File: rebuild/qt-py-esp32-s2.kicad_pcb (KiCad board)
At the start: 2 copper layers, 0 parts

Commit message: gate3: PCB placement — 45/45 placed, 17.78x20.701 outline, DRC run
- qt-py footprint library extracted from the imported board (14 footprints)
- pad names preserved: A/A'/B/B', 1C..7C, A1B12/A4B9/A6/B6, MT1/MT2, C/A, 1/3, FP, P$1, TP
- create_board_from_schematic: 45 footprints, 34 nets, 159 pads assigned
- placement copied from the imported board: 45/45 exact x/y/rotation/layer
- outline 17.78 x 20.701 (8 Edge.Cuts segments), 2 fiducials, no frame
- Eagle rules: 6 mil clearance/width, 15.5 mil drill, 25% annulus, 0.254 edge, 2L 1.6mm
- fixed castellation pad rotation (importer stored 270/90): shorts 26 -> 2
- ERC footprint_link_issues 17 -> 0; annotation warning cleared via GND0/VBAT0
- DRC: 236 violations (37 errors, 199 warnings), 111 unconnected (unrouted)
- renders: 3D top/bottom, 2D
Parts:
- added C1: 22uF, Capacitor_SMD:C_0805_2012Metric, F.Cu at (11.9, -12.7)
- added C10: 0.1uF, Capacitor_SMD:C_0402_1005Metric, B.Cu at (8.43, -14.2)
- added C11: 0.1uF, Capacitor_SMD:C_0402_1005Metric, B.Cu at (14.7, -15.1)
- added C12: 0.1uF, Capacitor_SMD:C_0402_1005Metric, B.Cu at (14.7, -10.9)
- added C13: 1uF, Capacitor_SMD:C_0402_1005Metric, B.Cu at (14.7, -12.9)
- added C14: 0.1uF, Capacitor_SMD:C_0402_1005Metric, B.Cu at (13.0, -2.29)
- added C15: 1uF, Capacitor_SMD:C_0402_1005Metric, B.Cu at (8.84, -3.62)
- added C16: 100pF, Capacitor_SMD:C_0402_1005Metric, B.Cu at (7.95, -3.62)
- added C17: 16pF, Capacitor_SMD:C_0402_1005Metric, B.Cu at (8.48, -2.08)
- added C18: 16pF, Capacitor_SMD:C_0402_1005Metric, B.Cu at (12.1, -2.26)
- added C19: 1uF, Capacitor_SMD:C_0402_1005Metric, B.Cu at (6.48, -14.0)
- added C2: 1uF, Capacitor_SMD:C_0402_1005Metric, B.Cu at (4.38, -9.86)
- added C20: 1uF, Capacitor_SMD:C_0402_1005Metric, B.Cu at (3.11, -12.9)
- added C3: 1uF, Capacitor_SMD:C_0402_1005Metric, B.Cu at (14.3, -2.10)
- added C4: 0.1uF, Capacitor_SMD:C_0402_1005Metric, B.Cu at (4.36, -8.92)
- added C5: 1uF, Capacitor_SMD:C_0402_1005Metric, B.Cu at (7.45, -14.2)
- added C6: 22uF, Capacitor_SMD:C_0805_2012Metric, F.Cu at (13.4, -9.80)
- added C7: TBD, Capacitor_SMD:C_0402_1005Metric, B.Cu at (4.17, -6.91)
- added C8: 22uF, Capacitor_SMD:C_0805_2012Metric, F.Cu at (10.5, -6.93)
- added C9: TBD, Capacitor_SMD:C_0402_1005Metric, B.Cu at (4.18, -5.78)
- added CONN1: STEMMA_I2C_QTSKINNY, qt-py:JST_SH4_SKINNY, F.Cu at (11.1, -2.58)
- added D1: NSR0320, qt-py:SOD-323_MINI, B.Cu at (12.5, -16.8)
- added D2: NSR0320, qt-py:SOD-323_MINI, B.Cu at (14.4, -18.9)
- added FID1: FIDUCIAL_1MM, qt-py:FIDUCIAL_1MM, F.Cu at (6.20, -19.5)
- added FID2: FIDUCIAL_1MM, qt-py:FIDUCIAL_1MM, F.Cu at (10.9, -0.76)
- added GND0: TESTPOINT_P, qt-py:TESTPOINT_MINUS_1X3MM, B.Cu at (6.99, -18.9)
- added JP1: HEADER_1X7, qt-py:1X07_CASTEL, F.Cu at (1.27, -10.4)
- added JP3: HEADER_1X7, qt-py:1X07_CASTEL, F.Cu at (16.5, -10.4)
- added L1: 2nH, Inductor_SMD:L_0402_1005Metric, B.Cu at (4.50, -7.92)
- added L2: 0 ohm, Inductor_SMD:L_0402_1005Metric, B.Cu at (5.69, -6.26)
- added LED1: WS2812B_SK6805_1515, qt-py:SK6805_1515, F.Cu at (13.1, -7.00)
- added Q1: BOOT0, qt-py:BTN_KMR2_4.6X2.8, F.Cu at (6.10, -11.0)
- added Q2: reset, qt-py:BTN_KMR2_4.6X2.8, F.Cu at (6.10, -7.11)
- added R1: 10K, Resistor_SMD:R_0402_1005Metric, B.Cu at (14.3, -2.98)
- added R17: 1Meg, Resistor_SMD:R_0402_1005Metric, B.Cu at (4.00, -12.9)
- added R2: 10K, Resistor_SMD:R_0402_1005Metric, B.Cu at (3.51, -17.1)
- added R3: 0, Resistor_SMD:R_0402_1005Metric, B.Cu at (10.6, -4.58)
- added R5: 5.1K, Resistor_SMD:R_0402_1005Metric, F.Cu at (7.30, -13.1)
- added R6: 5.1K, Resistor_SMD:R_0402_1005Metric, F.Cu at (9.27, -12.9)
- added SWC1: TPB1,27, qt-py:B1_27, B.Cu at (15.6, -0.95)
- added SWC2: TPB1,27, qt-py:B1_27, B.Cu at (2.26, -19.7)
- added U$15: ESP32-S2FN4R2, qt-py:QFN56_7X7, B.Cu at (10.3, -9.19)
- added U1: AP2112K-3.3, qt-py:SOT23-5, F.Cu at (10.9, -9.87)
- added VBAT0: TESTPOINT_P, qt-py:TESTPOINT_PLUS_1X3MM, B.Cu at (10.8, -18.9)
- added X1: ANTENNA_FP, qt-py:ANT_2450AT18B100, F.Cu at (4.83, -1.33)
- added X6: USB TYPE C, qt-py:USB_C_CUSB31-CFM2AX-01-X, F.Cu at (8.89, -17.9)
- added Y1: 40MHz, qt-py:CRYSTAL_2X1.6, B.Cu at (10.5, -2.77)
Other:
- board outline added: 17.8 x 20.7 mm

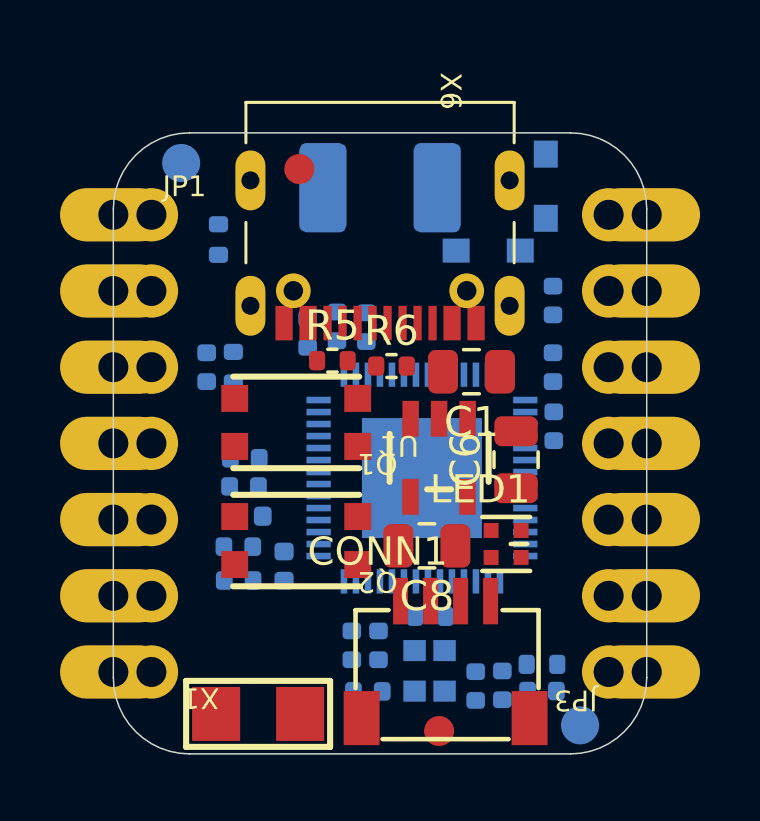
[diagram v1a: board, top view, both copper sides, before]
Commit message: gate4: routing — 0 DRC errors, 20 unconnected documented
preconditions:
- testpoint no-net copper polygon -> equivalent P$1 pad; courtyard closed
- removed ${TP_SIGNAL_NAME} from B1_27 and placed SWC instances
- USB-C NPTH resized 1.158 -> 0.65 mm to match Eagle drill
- documented waivers: castellation edge, USB-C internal holes, courtyard overlap

routing:
- Freerouting 2.5.0, 200 passes, 18 threads; 125 -> 24 unrouted; SES imported
- GND pours on F.Cu/B.Cu, solid pad connection
- 323 segments, 18 vias, 298.86 mm total
- DRC 0 errors, 196 cosmetic warnings, 20 unconnected (13 GND, 4 +3V3, 2 VBUS, 1 IO0)

honest shortfall:
- 20 connections remain unrouted; not intentional
- D+/D- skew 3.51 mm (original 1.10 mm), not length-matched
- lower total length reflects missing links + poured GND, not a better layout
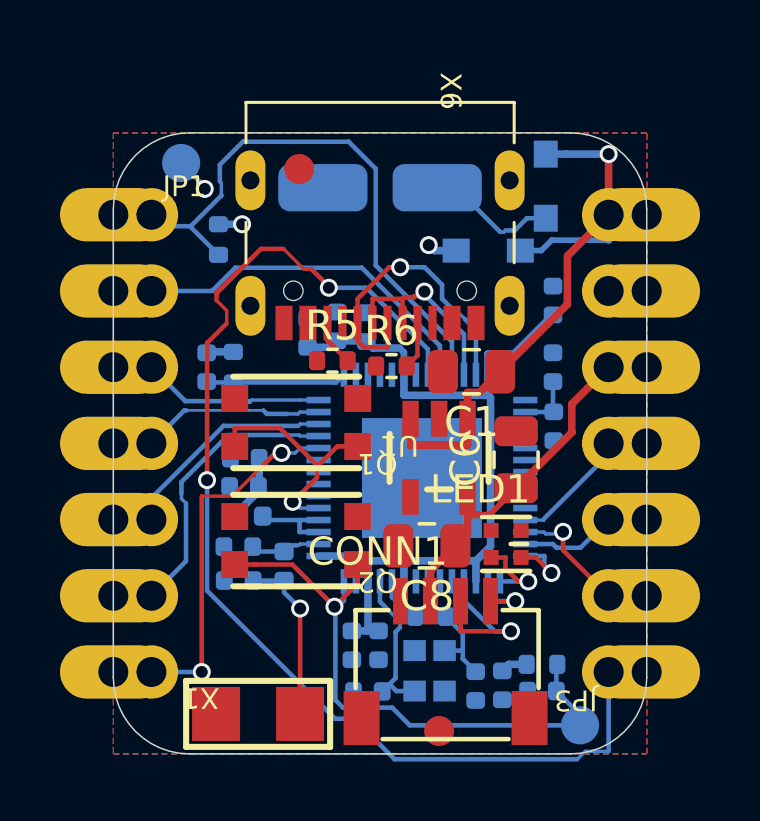
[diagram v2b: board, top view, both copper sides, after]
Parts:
- GND0: value TESTPOINT_P -> TESTPOINT_MINUS_1X3MM
- VBAT0: value TESTPOINT_P -> TESTPOINT_PLUS_1X3MM
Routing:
- net +3V3: track 0.00 -> 44.0 mm, vias 0 -> 1
- net RX: track 0.00 -> 40.0 mm, vias 0 -> 2
- net +5V: track 0.00 -> 22.0 mm, vias 0 -> 1
- net RESET_N: track 0.00 -> 20.7 mm, vias 0 -> 1
- net A0: track 0.00 -> 20.4 mm
- net TX: track 0.00 -> 13.4 mm, vias 0 -> 2
- net A1: track 0.00 -> 13.2 mm
- net SCL: track 0.00 -> 10.8 mm
- net D+: track 0.00 -> 10.3 mm, vias 0 -> 1
- net IO0: track 0.00 -> 9.27 mm, vias 0 -> 2
- net SDA: track 0.00 -> 8.58 mm
- net A3: track 0.00 -> 7.37 mm
- net A2: track 0.00 -> 7.35 mm
- net D-: track 0.00 -> 6.79 mm, vias 0 -> 1
- net RF_ANT: track 0.00 -> 5.70 mm, vias 0 -> 1
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- added copper zone on B.Cu, net GND
- added copper zone on F.Cu, net GND

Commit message: gate4b WIP: GND stitching 20->14, blocked on pour-island links
- 7 stitching vias at F/B fill intersections; main pours merged
- cleared CONN1.MT1/C17.2 and X6 zone links
- 20 -> 14 unconnected, 0 DRC errors, no new waivers
- remaining 7 GND links separated by our signal tracks; need signal reroute
- +3V3 reference geometry tried: 13 unconnected but 36 errors; reverted
- USB-C NPTH 0.65 mm source reference retained
- still NOT COMPLETE; no Gerbers/fabrication
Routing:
- net GND: vias 0 -> 8
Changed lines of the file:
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@@
 		(net "+5V")
+	)
+	(via
+		(at 8 -11.5)
+		(size 0.6)
+		(drill 0.4)
+		(layers "F.Cu" "B.Cu")
+		(net "GND")
+	)
+	(via
+		(at 8 -7.5)
+		(size 0.6)
+		(drill 0.4)
+		(layers "F.Cu" "B.Cu")
+		(net "GND")
+	)
+	(via
+		(at 11 -11)
+		(size 0.6)
+		(drill 0.4)
+		(layers "F.Cu" "B.Cu")
+		(net "GND")
+	)
+	(via
+		(at 4 -13.5)
+		(size 0.6)
+		(drill 0.4)
+		(layers "F.Cu" "B.Cu")
+		(net "GND")
+	)
+	(via
+		(at 12.5 -2)
+		(size 0.6)
+		(drill 0.4)
+		(layers "F.Cu" "B.Cu")
+		(net "GND")
+	)
+	(via
+		(at 8 -2.5)
+		(size 0.6)
+		(drill 0.4)
+		(layers "F.Cu" "B.Cu")
+		(net "GND")
+	)
+	(via
+		(at 8.5 -11.5)
+		(size 0.6)
+		(drill 0.4)
+		(layers "F.Cu" "B.Cu")
+		(net "GND")
+	)
+	(via
+		(at 15 -13.5)
+		(size 0.6)
+		(drill 0.4)
+		(layers "F.Cu" "B.Cu")
+		(net "GND")
 	)
 	(segment

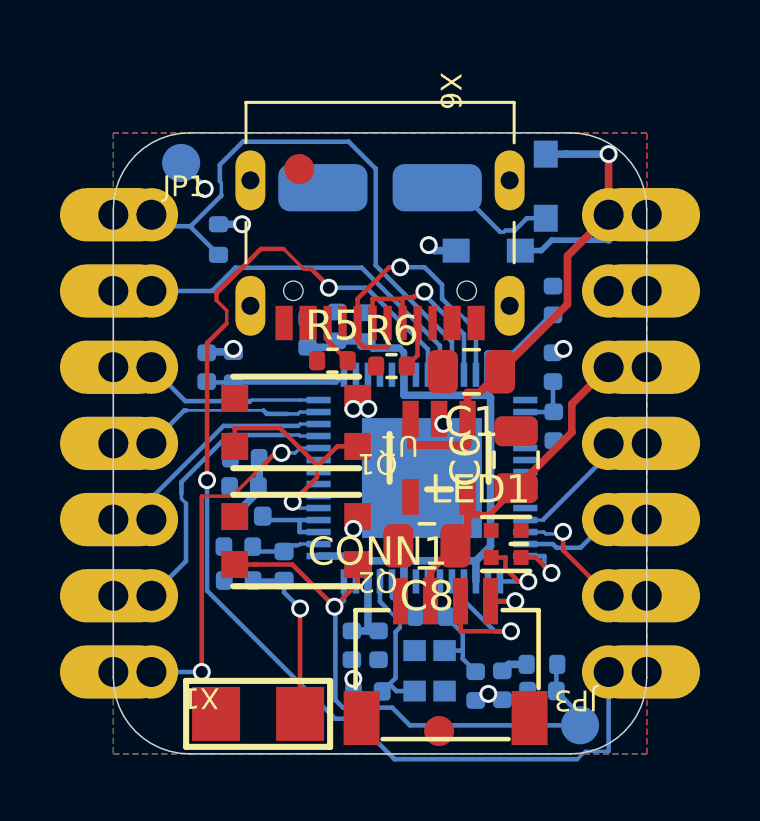
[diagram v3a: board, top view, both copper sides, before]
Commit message: gate4b: option 2 stalls at 9 unconnected / 0 errors
- reference power/GND mesh protected in DSN; Freerouting 11 unrouted
- imported SES, vias fixed: 13/0; pour stitching: 9/0
- reference signal corridors for last six nets: 5 unconnected but 39 errors; reverted
- remaining 9: 1 GND island pair, 2 +3V3 gaps, D+/A0/SDA/TX/RX/MISO pad escapes
- USB skew still 3.51 mm, not tuned
- both option 1 and option 2 exhausted under no-wholesale-copy
- NOT COMPLETE; no Gate 5, no Gerbers
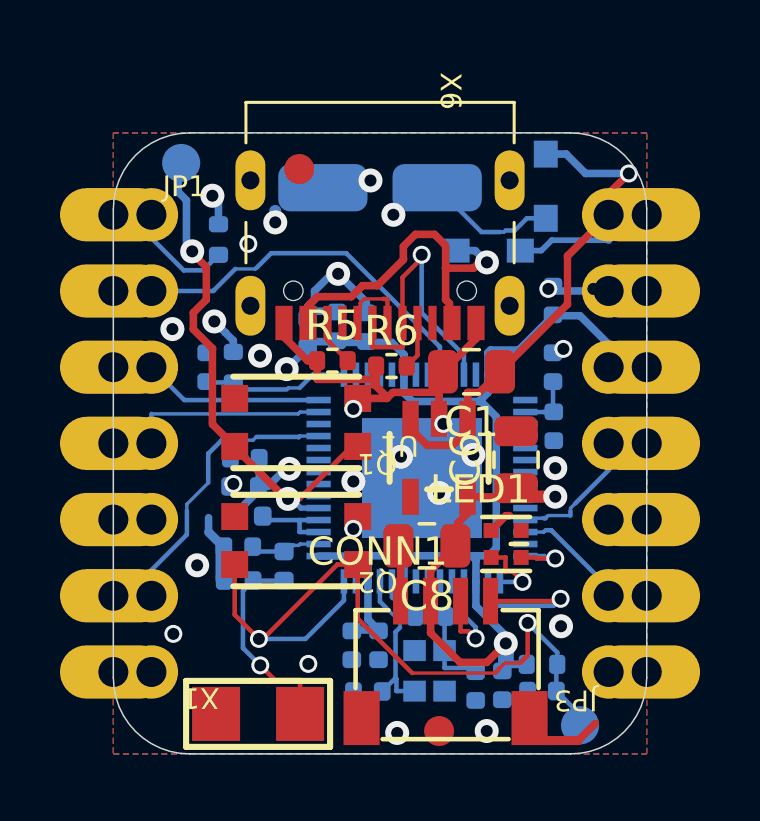
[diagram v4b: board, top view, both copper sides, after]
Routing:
- net RX: track 40.0 -> 0.00 mm, vias 2 -> 0
- net GND: track 0.90 -> 29.1 mm, vias 8 -> 25
- net A0: track 20.4 -> 4.94 mm
- net TX: track 13.4 -> 1.27 mm, vias 2 -> 0
- net +3V3: track 44.0 -> 55.9 mm, vias 1 -> 5
- net VBUS: track 0.99 -> 11.9 mm
- net IO0: track 9.27 -> 17.3 mm
- net D+: track 10.3 -> 2.48 mm, vias 1 -> 0
- net SDA: track 8.58 -> 1.27 mm
- net MISO: track 4.49 -> 0.00 mm
- net RESET_N: track 20.7 -> 24.9 mm, vias 1 -> 2
- net SCL1: track 2.38 -> 5.58 mm
- net D-: track 6.79 -> 9.73 mm
- net VBAT: track 4.42 -> 6.25 mm, vias 0 -> 1
- net SDA1: track 5.31 -> 3.76 mm
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
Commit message: gate4b/gate5: PASS as verified reconstruction; manufacturing outputs
- 4-layer source-faithful stack (In1 GND, In2 3.3V) approved; planes added
- reference zones restored; solid zone_connect on C15.2/C3.2/R6.1
- full reference signal routing fallback applied (approved)
- DRC 0 errors / 0 unconnected; D+ 9.238, D- 8.145, skew 1.093 mm
- C7/C9 marked DNP in schematic/board/BOM/PnP
- Gerbers (4 copper), PTH/NPTH drill, BOM, pos, stats, 2D/3D renders
- no fabrication, no ordering, no unconnected/DRC waivers
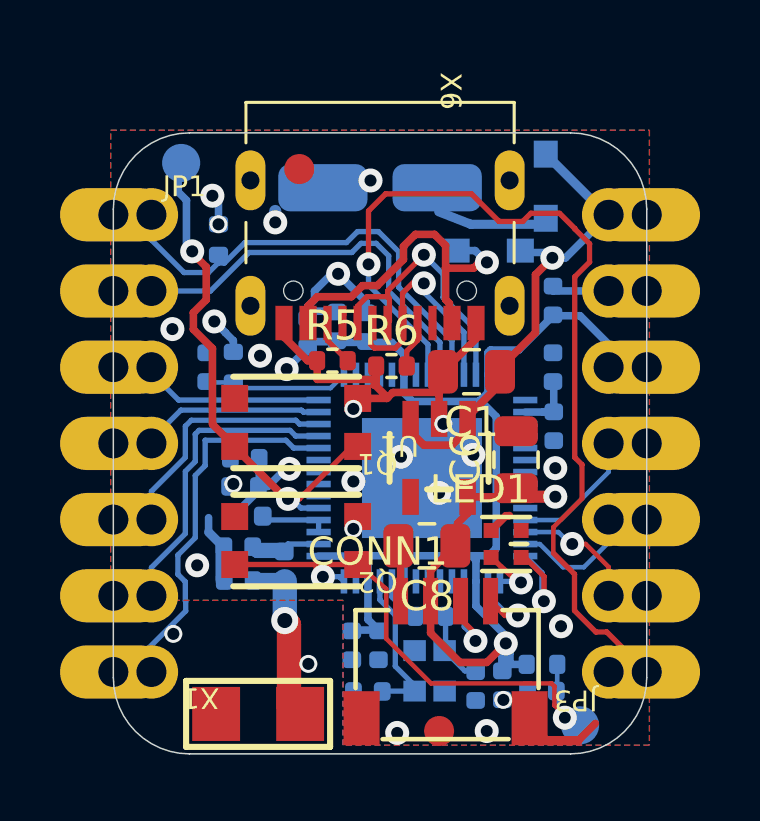
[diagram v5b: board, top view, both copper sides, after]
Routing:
- net RX: track 0.00 -> 32.6 mm, vias 0 -> 1
- net TX: track 1.27 -> 14.2 mm, vias 0 -> 1
- net A0: track 4.94 -> 16.8 mm
- net SDA: track 1.27 -> 9.43 mm
- net D+: track 2.48 -> 9.24 mm, vias 0 -> 1
- net RESET_N: track 24.9 -> 18.4 mm
- net MISO: track 0.00 -> 5.47 mm
- net +5V: track 21.9 -> 17.9 mm
- net SCL1: track 5.58 -> 2.85 mm
- net VBAT: track 6.25 -> 3.73 mm, vias 1 -> 0
- net D-: track 9.73 -> 8.14 mm
- net NEOPIX_PWR: track 2.18 -> 3.75 mm
- net RF_ANT: track 6.90 -> 5.75 mm, vias 1 -> 2
- net A1: track 13.6 -> 14.7 mm
- net SCL: track 10.7 -> 11.5 mm
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- added copper zone on In2.Cu, net +3V3
- added copper zone on In1.Cu, net GND
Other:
- copper layers 2 -> 4
